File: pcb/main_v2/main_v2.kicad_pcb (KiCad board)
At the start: 2 copper layers, 79.4 x 53.3 mm, 21 parts, among them J1 AS5600, J2 Btn, Q1 DMN3051L, SW1 SW_Push, SW2 SW_Push, U2 24AA02-OT, U3 PCA9536D

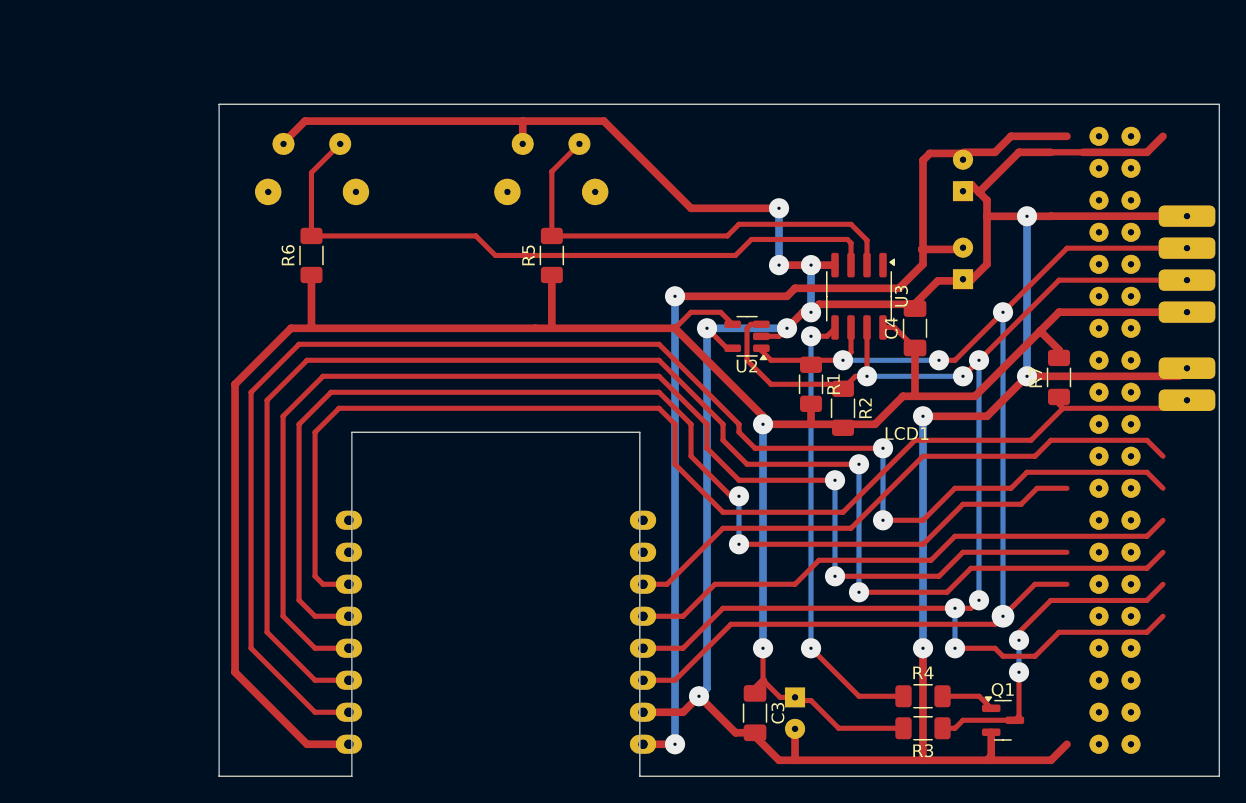
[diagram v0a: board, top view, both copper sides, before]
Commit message: pcb - lcd on wrong side
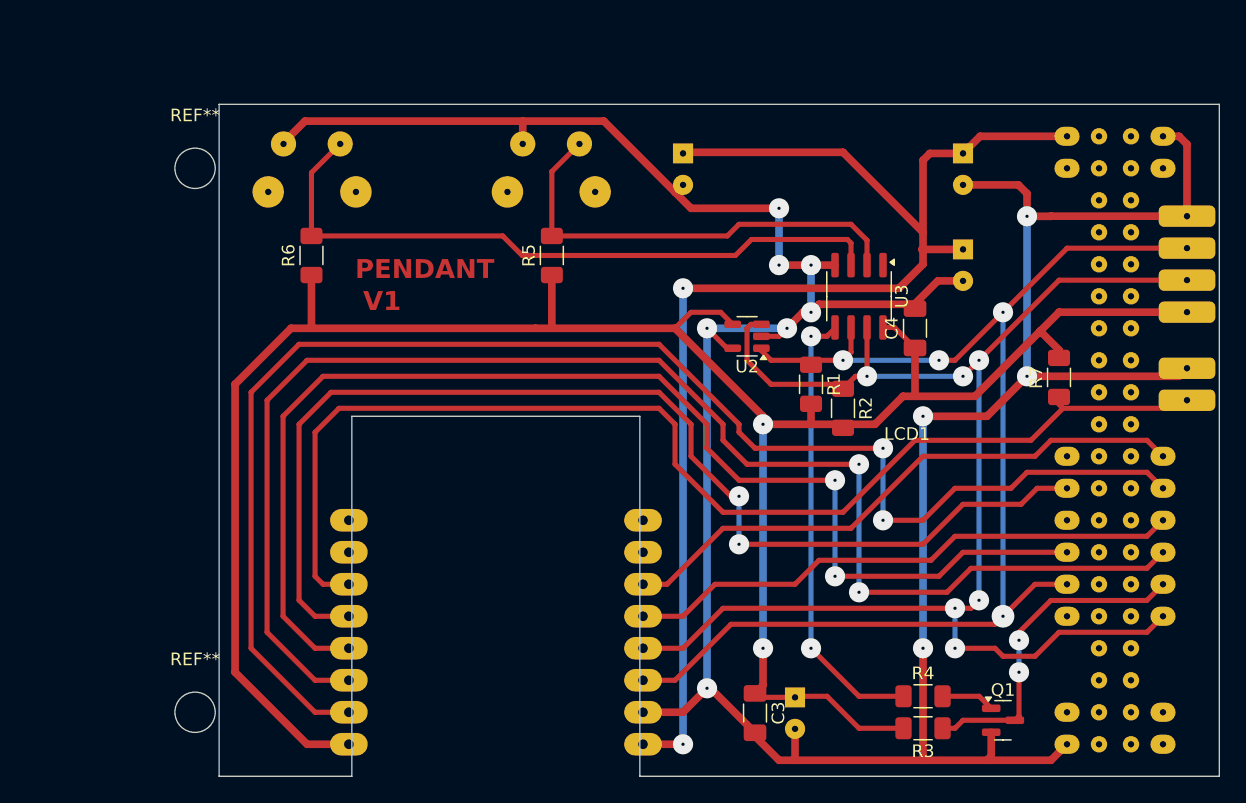
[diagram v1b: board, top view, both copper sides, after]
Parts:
- added C6: 100uF, Capacitor_THT:CP_Radial_D6.3mm_P2.50mm, B.Cu at (94.0, 54.7)
- added REF**: MountingHole_3.2mm_M3, MountingHole:MountingHole_3.2mm_M3, F.Cu at (55.2, 55.9)
- added REF**: MountingHole_3.2mm_M3, MountingHole:MountingHole_3.2mm_M3, F.Cu at (55.2, 99.1)
- moved C2 3.00 mm to (116.2, 54.7), turned to -90 degrees
- moved C5 2.36 mm to (116.2, 62.3), turned to -90 degrees
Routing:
- net /VIN: track 82.5 -> 104.7 mm
- net GNDD: track 259.1 -> 246.4 mm
- net /VCC_3_3: track 178.1 -> 179.0 mm
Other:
- outline, holes or cut-outs redrawn
- board text added: "PENDANT"
- board text added: "V1"

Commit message: pcb
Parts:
- LCD1: moved to B.Cu
- moved LCD1 76.7 mm to (42.3, 109.9)
- moved C2 50.1 mm to (98.1, 101.4), turned to 90 degrees
- moved C1 43.5 mm to (118.1, 57.1), turned to 90 degrees
- moved C6 40.9 mm to (103.2, 94.5), turned to 0 degrees
- moved C5 39.2 mm to (117.8, 101.4), turned to 90 degrees
- moved R3 35.9 mm to (121.3, 65.4), turned to -90 degrees
- moved Q1 35.6 mm to (118.1, 64.1)
- moved R4 34.9 mm to (113.7, 62.9)
- moved R7 22.4 mm to (117.5, 94.0), turned to -90 degrees
- moved J1 20.3 mm to (134.0, 87.6)
- moved J2 20.3 mm to (134.0, 92.0)
- moved C3 16.1 mm to (115.6, 96.5)
- moved R2 1.90 mm to (108.6, 74.9)
- moved C4 0.64 mm to (112.4, 67.9)
- moved R1 0.64 mm to (104.8, 73.0)
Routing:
- net /VIN: track 104.7 -> 40.6 mm
- net Net-(U3-IO3): track 35.2 -> 15.6 mm
- net Net-(LCD1-LCD_BACKL): track 26.1 -> 13.8 mm, vias 2 -> 0
- net Net-(LCD1-LCD_DC): track 44.4 -> 55.1 mm, vias 0 -> 2
- net /VCC_3_3: track 179.0 -> 189.6 mm, vias 2 -> 4
- net GNDD: track 246.4 -> 236.7 mm, vias 11 -> 12
- net Net-(J2-Pin_2): track 93.5 -> 100.1 mm, vias 0 -> 2
- net Net-(LCD1-LCD_CS): track 115.8 -> 109.4 mm, vias 2 -> 0
- net Net-(LCD1-LCD_SDI): track 114.6 -> 111.4 mm
- net Net-(Q1-G): track 4.26 -> 1.64 mm
- net Net-(LCD1-RST): track 46.5 -> 48.5 mm
- net /SCL: track 101.8 -> 100.3 mm, vias 4 -> 6
- net Net-(LCD1-LCD_SDO): track 98.7 -> 99.7 mm
- net Net-(LCD1-LCD_CLK): track 91.0 -> 90.4 mm
- net /SDA: track 115.2 -> 115.5 mm, vias 6 -> 4
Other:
- board text added: "V1.1"
- board text removed: "V1"
